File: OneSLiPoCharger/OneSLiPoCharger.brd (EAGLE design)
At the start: 101.6 x 52.1 mm, 54 parts, among them IC1 LM358N, Q1 BUZ10

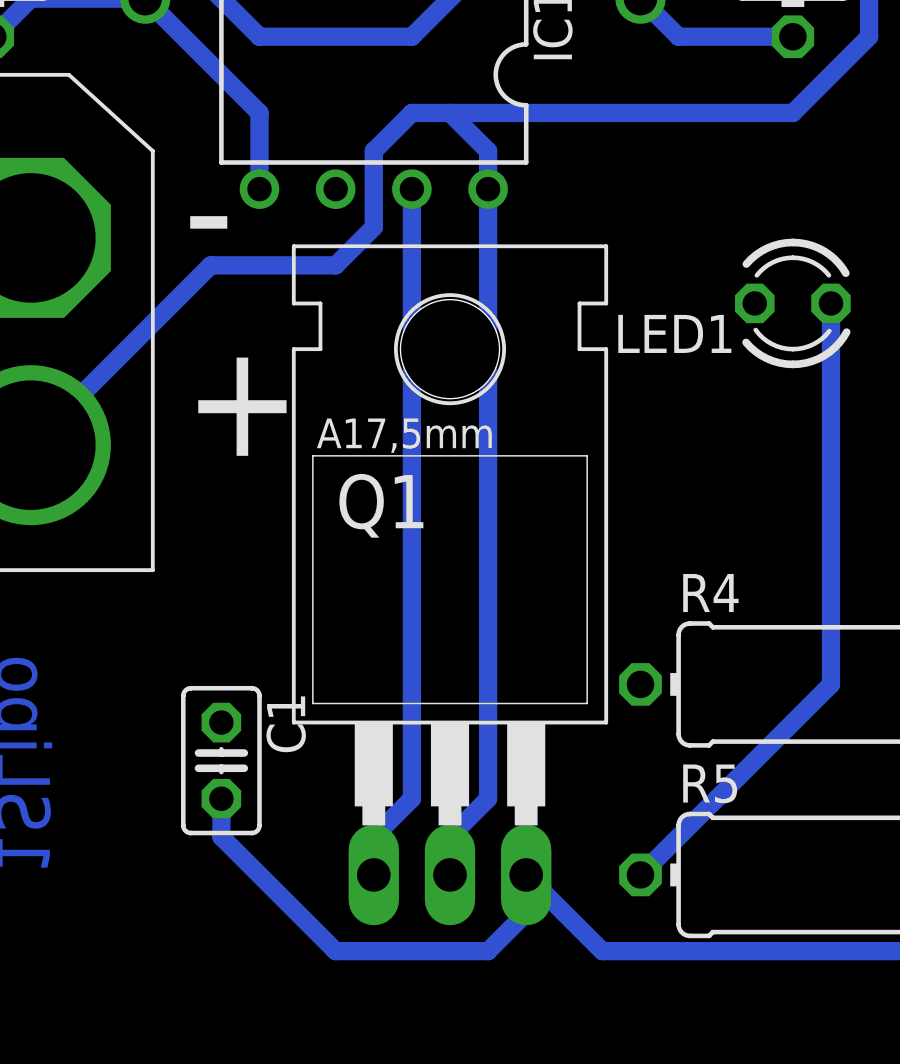
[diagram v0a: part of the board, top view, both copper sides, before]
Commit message: Pull in updates to Picoblade library
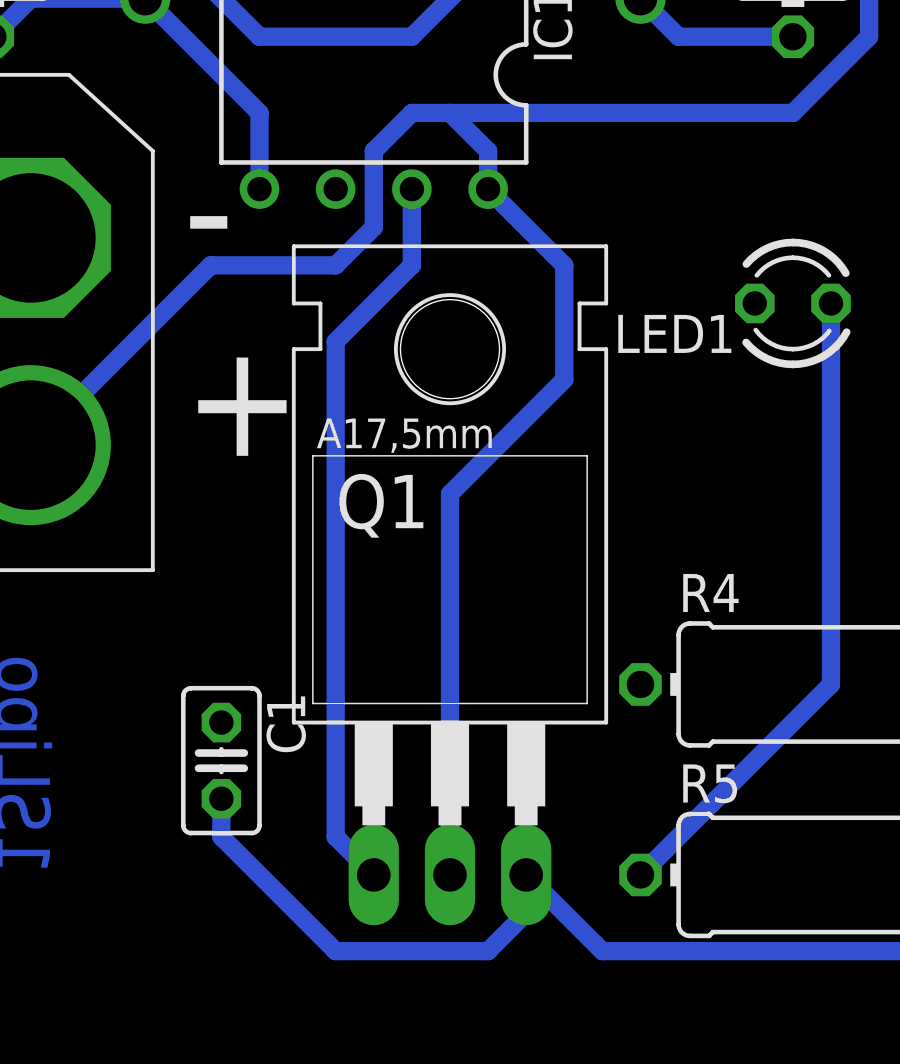
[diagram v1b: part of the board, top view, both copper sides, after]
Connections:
- net N$50 renamed GND
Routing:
- net VCC: track 87.8 -> 89.9 mm
- net N$5: track 23.4 -> 24.4 mm
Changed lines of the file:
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@@
 <grid distance="0.05" unitdist="inch" unit="inch" style="lines" multiple="1" display="no" altdistance="0.025" altunitdist="inch" altunit="inch"/>
 <layers>
-<layer number="1" name="Top" color="4" fill="1" visible="no" active="yes"/>
+<layer number="1" name="Top" color="4" fill="1" visible="yes" active="yes"/>
 <layer number="16" name="Bottom" color="1" fill="1" visible="yes" active="yes"/>
 <layer number="17" name="Pads" color="2" fill="1" visible="yes" active="yes"/>
 <layer number="18" name="Vias" color="2" fill="1" visible="yes" active="yes"/>
-<layer number="19" name="Unrouted" color="6" fill="1" visible="no" active="yes"/>
+<layer number="19" name="Unrouted" color="6" fill="1" visible="yes" active="yes"/>
 <layer number="20" name="Dimension" color="15" fill="1" visible="yes" active="yes"/>
-<layer number="21" name="tPlace" color="7" fill="1" visible="no" active="yes"/>
-<layer number="22" name="bPlace" color="7" fill="1" visible="no" active="yes"/>
-<layer number="23" name="tOrigins" color="15" fill="1" visible="no" active="yes"/>
-<layer number="24" name="bOrigins" color="15" fill="1" visible="no" active="yes"/>
+<layer number="21" name="tPlace" color="7" fill="1" visible="yes" active="yes"/>
+<layer number="22" name="bPlace" color="7" fill="1" visible="yes" active="yes"/>
+<layer number="23" name="tOrigins" color="15" fill="1" visible="yes" active="yes"/>
+<layer number="24" name="bOrigins" color="15" fill="1" visible="yes" active="yes"/>
 <layer number="25" name="tNames" color="7" fill="1" visible="no" active="yes"/>
 <layer number="26" name="bNames" color="7" fill="1" visible="no" active="yes"/>
@@
 <layer number="28" name="bValues" color="7" fill="1" visible="no" active="yes"/>
 <layer number="29" name="tStop" color="7" fill="3" visible="no" active="yes"/>
-<layer number="30" name="bStop" color="7" fill="6" visible="no" active="yes"/>
+<layer number="30" name="bStop" color="11" fill="1" visible="yes" active="yes"/>
 <layer number="31" name="tCream" color="7" fill="4" visible="no" active="yes"/>
 <layer number="32" name="bCream" color="7" fill="5" visible="no" active="yes"/>
@@
 <wire x1="22.86" y1="31.75" x2="24.13" y2="30.48" width="0.6096" layer="16"/>
 <wire x1="24.13" y1="30.48" x2="24.13" y2="29.21" width="0.6096" layer="16"/>
-<wire x1="22.86" y1="6.35" x2="22.86" y2="7.62" width="0.6096" layer="16"/>
-<wire x1="22.86" y1="7.62" x2="24.13" y2="8.89" width="0.6096" layer="16"/>
-<wire x1="24.13" y1="8.89" x2="24.13" y2="29.21" width="0.6096" layer="16"/>
 <wire x1="22.86" y1="31.75" x2="34.29" y2="31.75" width="0.6096" layer="16"/>
 <wire x1="34.29" y1="31.75" x2="36.83" y2="34.29" width="0.6096" layer="16"/>
 <wire x1="36.83" y1="34.29" x2="36.83" y2="41.91" width="0.6096" layer="16"/>
 <wire x1="36.83" y1="41.91" x2="34.29" y2="44.45" width="0.6096" layer="16"/>
-</signal>
-<signal name="N$50">
+<wire x1="22.86" y1="6.35" x2="22.86" y2="19.05" width="0.6096" layer="16"/>
+<wire x1="22.86" y1="19.05" x2="26.67" y2="22.86" width="0.6096" layer="16"/>
+<wire x1="26.67" y1="22.86" x2="26.67" y2="26.67" width="0.6096" layer="16"/>
+<wire x1="26.67" y1="26.67" x2="24.13" y2="29.21" width="0.6096" layer="16"/>
+</signal>
+<signal name="GND">
 <contactref element="R1" pad="A"/>
 <contactref element="D1" pad="A"/>
@@
 <contactref element="IC1" pad="7"/>
 <contactref element="Q1" pad="1"/>
-<wire x1="21.59" y1="29.21" x2="21.59" y2="8.89" width="0.6096" layer="16"/>
-<wire x1="21.59" y1="8.89" x2="20.32" y2="7.62" width="0.6096" layer="16"/>
-<wire x1="20.32" y1="7.62" x2="20.32" y2="6.35" width="0.6096" layer="16"/>
+<wire x1="21.59" y1="29.21" x2="21.59" y2="26.67" width="0.6096" layer="16"/>
+<wire x1="21.59" y1="26.67" x2="19.05" y2="24.13" width="0.6096" layer="16"/>
+<wire x1="19.05" y1="24.13" x2="19.05" y2="7.62" width="0.6096" layer="16"/>
+<wire x1="19.05" y1="7.62" x2="20.32" y2="6.35" width="0.6096" layer="16"/>
 </signal>
 <signal name="+5V">

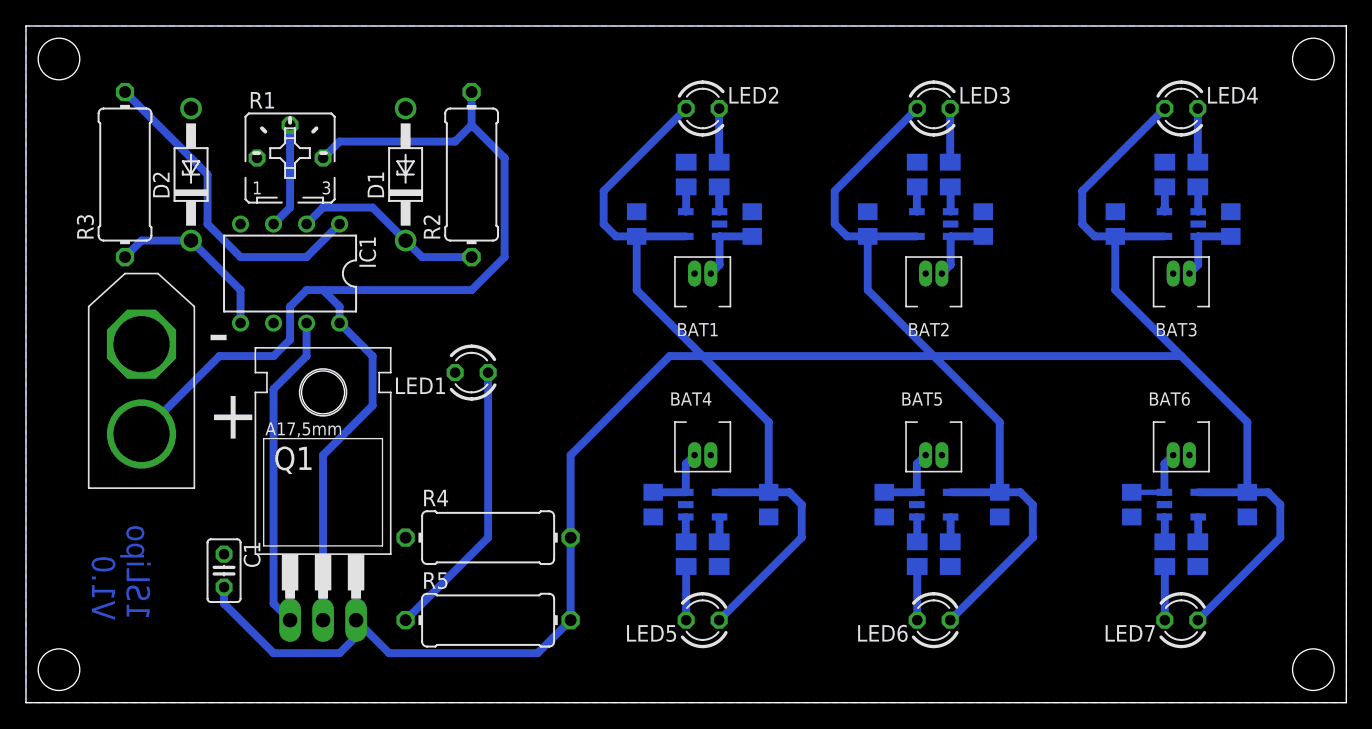
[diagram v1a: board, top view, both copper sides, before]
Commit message: Add a header for a voltmeter module.
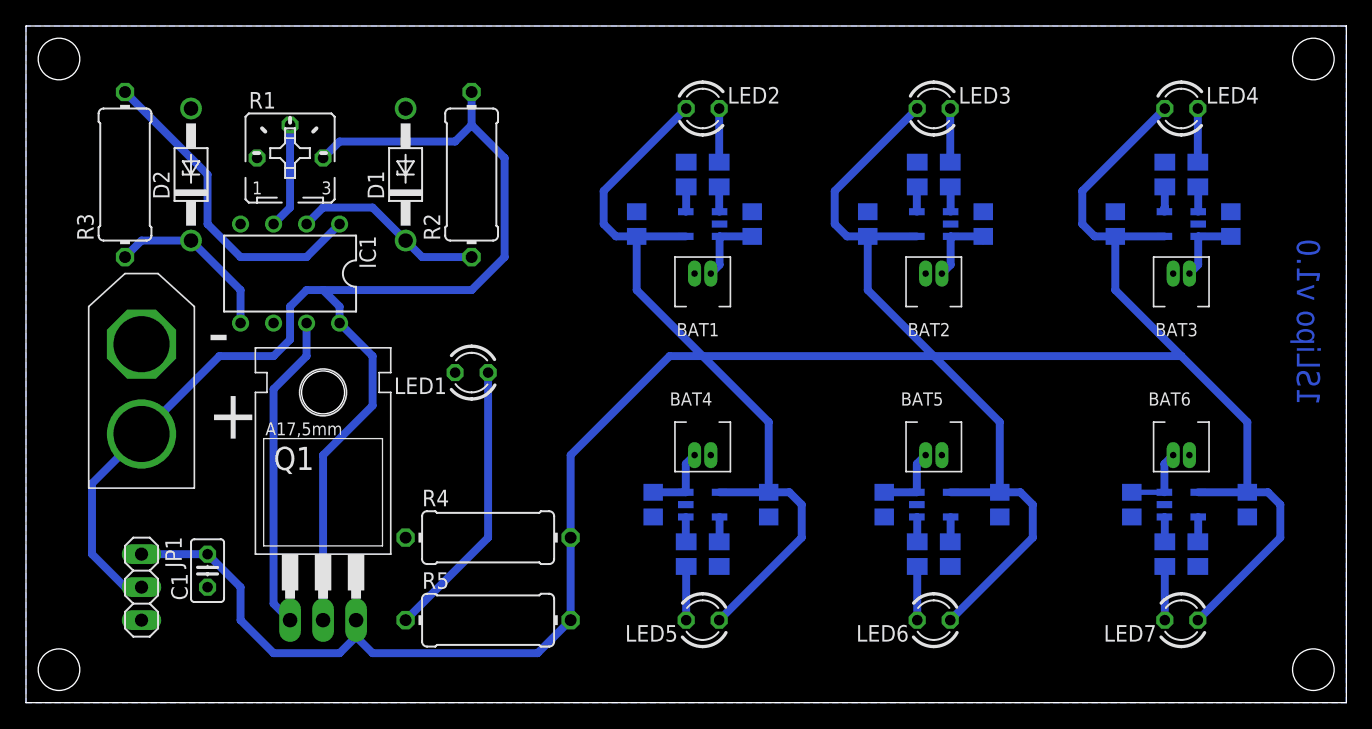
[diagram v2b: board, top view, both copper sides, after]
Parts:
- added JP1: (no value), pinhead:1X03
- moved C1 1.27 mm to (14.0, 10.2), turned to 90 degrees
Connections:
- net +5V: now also JP1.1
- net GND: now also JP1.3
- net VCC: now also JP1.2
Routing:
- net VCC: track 89.9 -> 105.5 mm
- net +5V: track 277.4 -> 285.0 mm
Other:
- board text added: "1SLipo v1.0"
- board text removed: "1SLipo V1.0"
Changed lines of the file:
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@@
 <text x="67.31" y="22.86" size="1.016" layer="21">BAT5</text>
 <text x="86.36" y="22.86" size="1.016" layer="21">BAT6</text>
-<text x="5.08" y="6.35" size="1.778" layer="16" rot="MR90">1SLipo
-V1.0</text>
+<text x="97.79" y="22.86" size="1.778" layer="16" rot="MR90">1SLipo v1.0</text>
 <hole x="2.54" y="2.54" drill="3.2"/>
 <hole x="2.54" y="49.53" drill="3.2"/>
@@
 </autorouter>
 <elements>
-<element name="C1" library="rcl" package="C025-025X050" value="" x="15.24" y="10.16" rot="R270"/>
+<element name="C1" library="rcl" package="C025-025X050" value="" x="13.97" y="10.16" rot="R90"/>
 <element name="C2" library="rcl" package="C0805" value="4.7uF" x="46.99" y="36.83" rot="MR90"/>
 <element name="C3" library="rcl" package="C0805" value="4.7uF" x="55.88" y="36.83" rot="MR270"/>
@@
 <element name="U$13" library="Picoblade" package="PICOBLADE-2PIN" value="PICOBLADE-2PIN" x="88.9" y="19.05" rot="R180"/>
 <element name="C13" library="rcl" package="C0805" value="4.7uF" x="85.09" y="15.24" rot="MR90"/>
+<element name="JP1" library="pinhead" package="1X03" value="" x="8.89" y="8.89" rot="R270"/>
 </elements>
 <signals>
@@
 <wire x1="26.67" y1="22.86" x2="26.67" y2="26.67" width="0.6096" layer="16"/>
 <wire x1="26.67" y1="26.67" x2="24.13" y2="29.21" width="0.6096" layer="16"/>
+<contactref element="JP1" pad="2"/>
+<wire x1="8.89" y1="20.6756" x2="5.08" y2="16.8656" width="0.6096" layer="16"/>
+<wire x1="5.08" y1="16.8656" x2="5.08" y2="11.43" width="0.6096" layer="16"/>
+<wire x1="5.08" y1="11.43" x2="7.62" y2="8.89" width="0.6096" layer="16"/>
+<wire x1="7.62" y1="8.89" x2="8.89" y2="8.89" width="0.6096" layer="16"/>
 </signal>
 <signal name="GND">
@@
 <contactref element="C13" pad="1"/>
 <contactref element="U$13" pad="P$1"/>
+<contactref element="JP1" pad="3"/>
 </signal>
 <signal name="N$1">
@@
 <contactref element="U$1" pad="4"/>
 <wire x1="41.91" y1="6.35" x2="41.91" y2="12.7" width="0.6096" layer="16"/>
-<wire x1="15.24" y1="8.89" x2="15.24" y2="7.62" width="0.6096" layer="16"/>
-<wire x1="15.24" y1="7.62" x2="19.05" y2="3.81" width="0.6096" layer="16"/>
-<wire x1="19.05" y1="3.81" x2="24.13" y2="3.81" width="0.6096" layer="16"/>
-<wire x1="24.13" y1="3.81" x2="25.4" y2="5.08" width="0.6096" layer="16"/>
-<wire x1="25.4" y1="5.08" x2="25.4" y2="6.35" width="0.6096" layer="16"/>
-<wire x1="25.4" y1="6.35" x2="27.94" y2="3.81" width="0.6096" layer="16"/>
-<wire x1="27.94" y1="3.81" x2="39.37" y2="3.81" width="0.6096" layer="16"/>
 <wire x1="39.37" y1="3.81" x2="41.91" y2="6.35" width="0.6096" layer="16"/>
 <wire x1="46.99" y1="35.88" x2="50.77" y2="35.88" width="0.6096" layer="16"/>
@@
 <wire x1="41.91" y1="19.05" x2="41.91" y2="12.7" width="0.6096" layer="16"/>
 <wire x1="49.53" y1="26.67" x2="52.07" y2="26.67" width="0.6096" layer="16"/>
+<contactref element="JP1" pad="1"/>
+<wire x1="8.89" y1="11.43" x2="13.97" y2="11.43" width="0.6096" layer="16"/>
+<wire x1="13.97" y1="11.43" x2="16.51" y2="8.89" width="0.6096" layer="16"/>
+<wire x1="16.51" y1="8.89" x2="16.51" y2="6.35" width="0.6096" layer="16"/>
+<wire x1="16.51" y1="6.35" x2="19.05" y2="3.81" width="0.6096" layer="16"/>
+<wire x1="19.05" y1="3.81" x2="24.13" y2="3.81" width="0.6096" layer="16"/>
+<wire x1="24.13" y1="3.81" x2="25.4" y2="5.08" width="0.6096" layer="16"/>
+<wire x1="25.4" y1="6.35" x2="25.4" y2="5.08" width="0.6096" layer="16"/>
+<wire x1="25.4" y1="5.08" x2="26.67" y2="3.81" width="0.6096" layer="16"/>
+<wire x1="26.67" y1="3.81" x2="39.37" y2="3.81" width="0.6096" layer="16"/>
 </signal>
 <signal name="N$10">
@@
 </board>
 </drawing>
-<compatibility>
-<note version="6.3" minversion="6.2.2" severity="warning">
-Since Version 6.2.2 text objects can contain more than one line,
-which will not be processed correctly with this version.
-</note>
-</compatibility>
 </eagle>
